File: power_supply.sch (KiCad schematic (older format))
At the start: 0 parts

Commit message: MSP73833 circuit stuff
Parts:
- added C? (x2): 4.7uF, symbol C
- added J?: USB, ~, symbol USB
- added LD? (x3): LED, ~, symbol LED
- added R? (x3): 1.5K, symbol R
- added R?: 1K, symbol R
- added RT?: 10K, symbol THERMISTOR
- added U?: MCP73833, ~, symbol MCP73833
- added U?: BATT, symbol BATT
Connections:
- net labels added: VBAT, VDD, VSS
- wire segments 0 -> 27
- no-connect marks 0 -> 3
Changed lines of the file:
@@
 LIBS:w_rtx
 LIBS:w_transistor
+LIBS:power_supply
 LIBS:power_supply-cache
 EELAYER 27 0
@@
 Comment4 ""
 $EndDescr
+$Comp
+L MCP73833 U?
+U 1 1 539B5EF0
+P 3500 2950
+F 0 "U?" H 3500 2650 60  0000 C CNN
+F 1 "MCP73833" H 3500 3250 60  0000 C CNN
+F 2 "~" H 3500 2800 60  0000 C CNN
+F 3 "~" H 3500 2800 60  0000 C CNN
+	1    3500 2950
+	1    0    0    -1
+$EndComp
+$Comp
+L USB J?
+U 1 1 539B5F0C
+P 1150 1250
+F 0 "J?" H 950 1250 60  0000 C CNN
+F 1 "USB" H 900 1600 60  0000 C CNN
+F 2 "~" H 1050 1350 60  0000 C CNN
+F 3 "~" H 1050 1350 60  0000 C CNN
+	1    1150 1250
+	1    0    0    -1
+$EndComp
+Text Label 1700 1450 0    60   ~ 0
+VSS
+Text Label 1700 1050 0    60   ~ 0
+VDD
+NoConn ~ 1600 1150
+NoConn ~ 1600 1250
+NoConn ~ 1600 1350
+Text Label 1900 2800 2    60   ~ 0
+VDD
+$Comp
+L C C?
+U 1 1 539B5F60
+P 2000 2900
+F 0 "C?" H 2050 2910 50  0000 L CNN
+F 1 "4.7uF" H 2050 2840 50  0000 L CNN
+F 2 "" H 2000 2900 60  0000 C CNN
+F 3 "" H 2000 2900 60  0000 C CNN
+	1    2000 2900
+	1    0    0    -1
+$EndComp
+Text Label 2000 3050 3    60   ~ 0
+VSS
+$Comp
+L C C?
+U 1 1 539B5FA3
+P 5100 2900
+F 0 "C?" H 5150 2910 50  0000 L CNN
+F 1 "4.7uF" H 5150 2840 50  0000 L CNN
+F 2 "" H 5100 2900 60  0000 C CNN
+F 3 "" H 5100 2900 60  0000 C CNN
+	1    5100 2900
+	1    0    0    -1
+$EndComp
+Text Label 5100 3050 3    60   ~ 0
+VSS
+$Comp
+L R R?
+U 1 1 539B5FBE
+P 2700 2950
+F 0 "R?" V 2750 2800 50  0000 C CNN
+F 1 "1.5K" V 2750 2950 50  0000 C CNN
+F 2 "" H 2700 2950 60  0000 C CNN
+F 3 "" H 2700 2950 60  0000 C CNN
+	1    2700 2950
+	0    -1   -1   0
+$EndComp
+$Comp
+L R R?
+U 1 1 539B5FCB
+P 2700 3050
+F 0 "R?" V 2750 2900 50  0000 C CNN
+F 1 "1.5K" V 2750 3050 50  0000 C CNN
+F 2 "" H 2700 3050 60  0000 C CNN
+F 3 "" H 2700 3050 60  0000 C CNN
+	1    2700 3050
+	0    -1   -1   0
+$EndComp
+$Comp
+L R R?
+U 1 1 539B5FD1
+P 4300 3050
+F 0 "R?" V 4350 2900 50  0000 C CNN
+F 1 "1.5K" V 4350 3050 50  0000 C CNN
+F 2 "" H 4300 3050 60  0000 C CNN
+F 3 "" H 4300 3050 60  0000 C CNN
+	1    4300 3050
+	0    1    1    0
+$EndComp
+$Comp
+L LED LD?
+U 1 1 539B6061
+P 2450 2950
+F 0 "LD?" H 2400 3000 40  0000 C CNN
+F 1 "LED" H 2550 3000 40  0000 C CNN
+F 2 "~" H 2450 2950 60  0000 C CNN
+F 3 "~" H 2450 2950 60  0000 C CNN
+	1    2450 2950
+	-1   0    0    1
+$EndComp
+$Comp
+L LED LD?
+U 1 1 539B6067
+P 2450 3050
+F 0 "LD?" H 2400 3100 40  0000 C CNN
+F 1 "LED" H 2550 3100 40  0000 C CNN
+F 2 "~" H 2450 3050 60  0000 C CNN
+F 3 "~" H 2450 3050 60  0000 C CNN
+	1    2450 3050
+	-1   0    0    1
+$EndComp
+$Comp
+L LED LD?
+U 1 1 539B606D
+P 4550 3050
+F 0 "LD?" H 4500 3100 40  0000 C CNN
+F 1 "LED" H 4650 3100 40  0000 C CNN
+F 2 "~" H 4550 3050 60  0000 C CNN
+F 3 "~" H 4550 3050 60  0000 C CNN
+	1    4550 3050
+	1    0    0    -1
+$EndComp
+$Comp
+L R R?
+U 1 1 539B617E
+P 4100 3350
+F 0 "R?" V 4150 3350 50  0000 C CNN
+F 1 "1K" V 4050 3350 50  0000 C CNN
+F 2 "" H 4100 3350 60  0000 C CNN
+F 3 "" H 4100 3350 60  0000 C CNN
+	1    4100 3350
+	1    0    0    -1
+$EndComp
+Text Label 4100 3550 3    60   ~ 0
+VSS
+Text Label 2800 3150 2    60   ~ 0
+VSS
+Text Label 4750 3050 0    60   ~ 0
+VDD
+Wire Wire Line
+	1600 1450 1700 1450
+Wire Wire Line
+	1600 1050 1700 1050
+Wire Wire Line
+	2900 2850 2900 2750
+Wire Wire Line
+	1900 2800 2900 2800
+Connection ~ 2900 2800
+Wire Wire Line
+	2000 2850 2000 2800
+Connection ~ 2000 2800
+Wire Wire Line
+	2000 3000 2000 3050
+Wire Wire Line
+	4100 2750 4100 2850
+Wire Wire Line
+	4100 2800 5650 2800
+Connection ~ 4100 2800
+Wire Wire Line
+	5100 2850 5100 2800
+Wire Wire Line
+	5100 3000 5100 3050
+Connection ~ 5100 2800
+Wire Wire Line
+	2900 2950 2800 2950
+Wire Wire Line
+	2800 3050 2900 3050
+Wire Wire Line
+	4100 3050 4200 3050
+Wire Wire Line
+	4400 3050 4450 3050
+Wire Wire Line
+	2550 3050 2600 3050
+Wire Wire Line
+	2600 2950 2550 2950
+Wire Wire Line
+	2350 2950 2350 2800
+Connection ~ 2350 2800
+Wire Wire Line
+	2300 2800 2300 3050
+Wire Wire Line
+	2300 3050 2350 3050
+Connection ~ 2300 2800
+Wire Wire Line
+	4650 3050 4750 3050
+Wire Wire Line
+	4100 3250 4100 3150
+Wire Wire Line
+	4100 3450 4100 3550
+Wire Wire Line
+	2900 3150 2800 3150
+Wire Wire Line
+	4100 2950 4200 2950
+$Comp
+L THERMISTOR RT?
+U 1 1 539B6353
+P 4400 2950
+F 0 "RT?" V 4450 2750 60  0000 C CNN
+F 1 "10K" V 4450 3050 60  0000 C CNN
+F 2 "" H 4400 2950 60  0000 C CNN
+F 3 "" H 4400 2950 60  0000 C CNN
+	1    4400 2950
+	0    -1   -1   0
+$EndComp
+Text Label 4750 2950 0    60   ~ 0
+VSS
+Wire Wire Line
+	4750 2950 4650 2950
+$Comp
+L BATT U?
+U 1 1 539B649A
+P 5600 2950
+F 0 "U?" V 5675 2925 60  0000 C CNN
+F 1 "BATT" V 5550 2925 60  0000 C CNN
+F 2 "" H 5600 2950 60  0000 C CNN
+F 3 "" H 5600 2950 60  0000 C CNN
+	1    5600 2950
+	1    0    0    -1
+$EndComp
+Wire Wire Line
+	5600 2800 5600 2850
+Text Label 5650 2800 0    60   ~ 0
+VBAT
+Connection ~ 5600 2800
+Text Label 5600 3150 3    60   ~ 0
+VSS
+Wire Wire Line
+	5600 3100 5600 3150
 $EndSCHEMATC

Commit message: Updated library. Began adding components.
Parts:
- added R?: 100k, symbol R
- added U?: FDC6392S, symbol FDC6392S
- added U?: MIC2185, symbol MIC2185
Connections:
- net labels added: VSYS
- wire segments 27 -> 35
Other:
- moved on the sheet: C?, J?, LD?, R?, RT?, U?

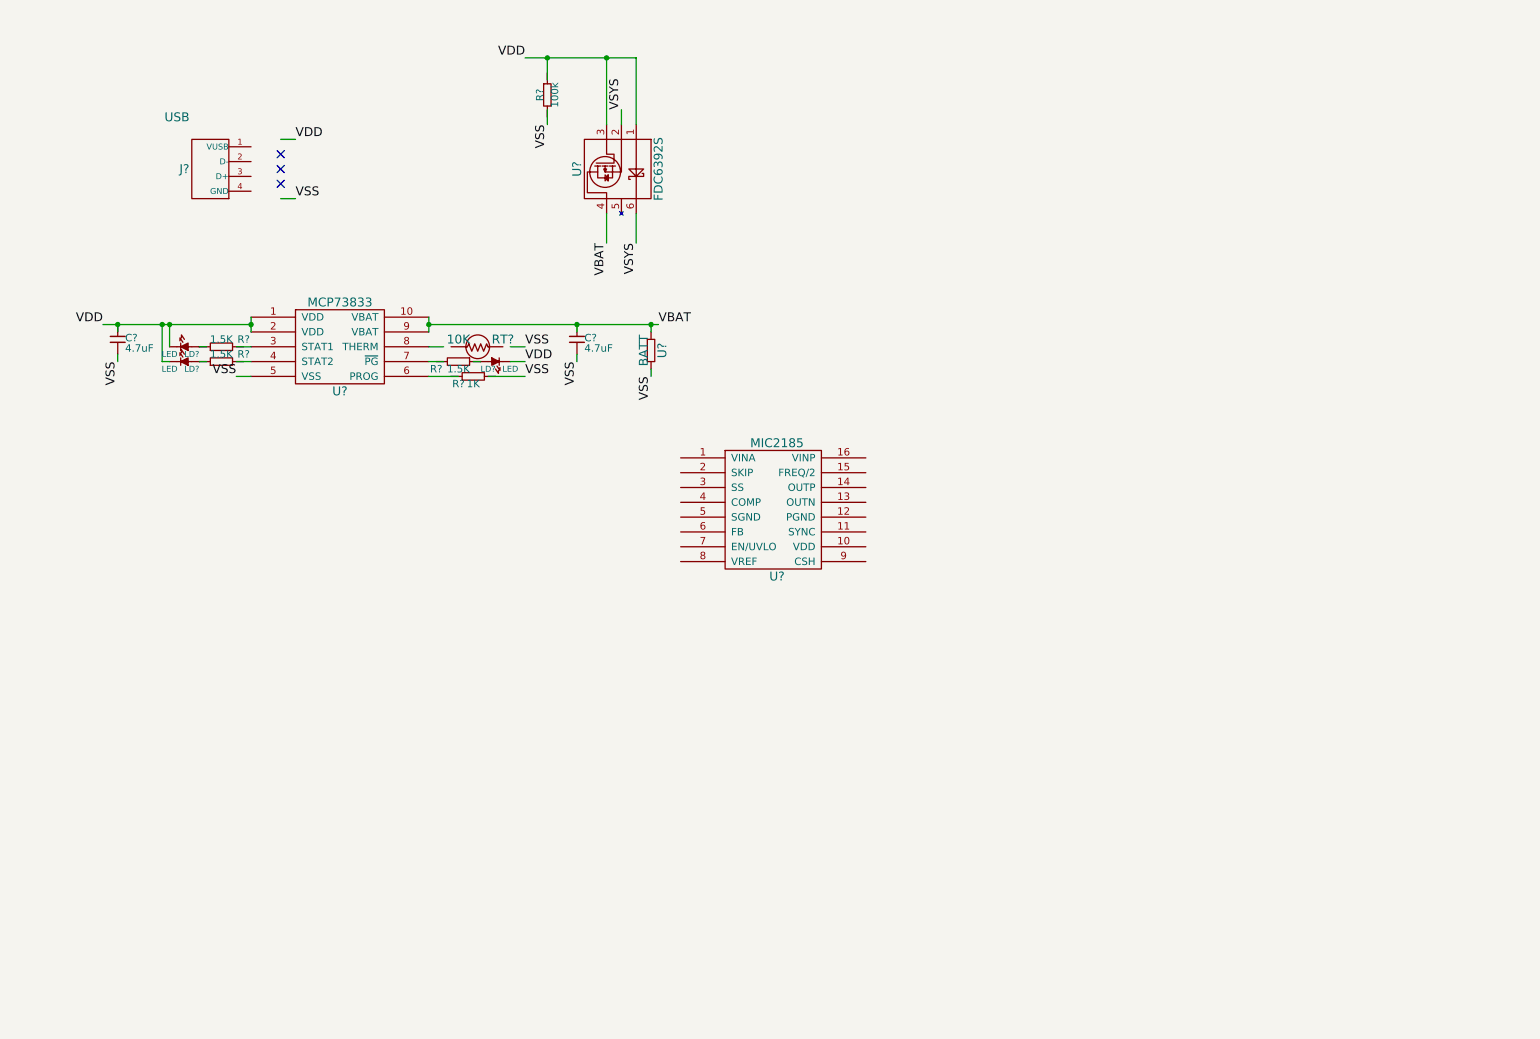
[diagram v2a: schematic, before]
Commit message: Power Supply Schematic
Completed schematic up through the MIC2185

Regulated output voltage named VpREG

Custom components listed in power_supply-cache.lib
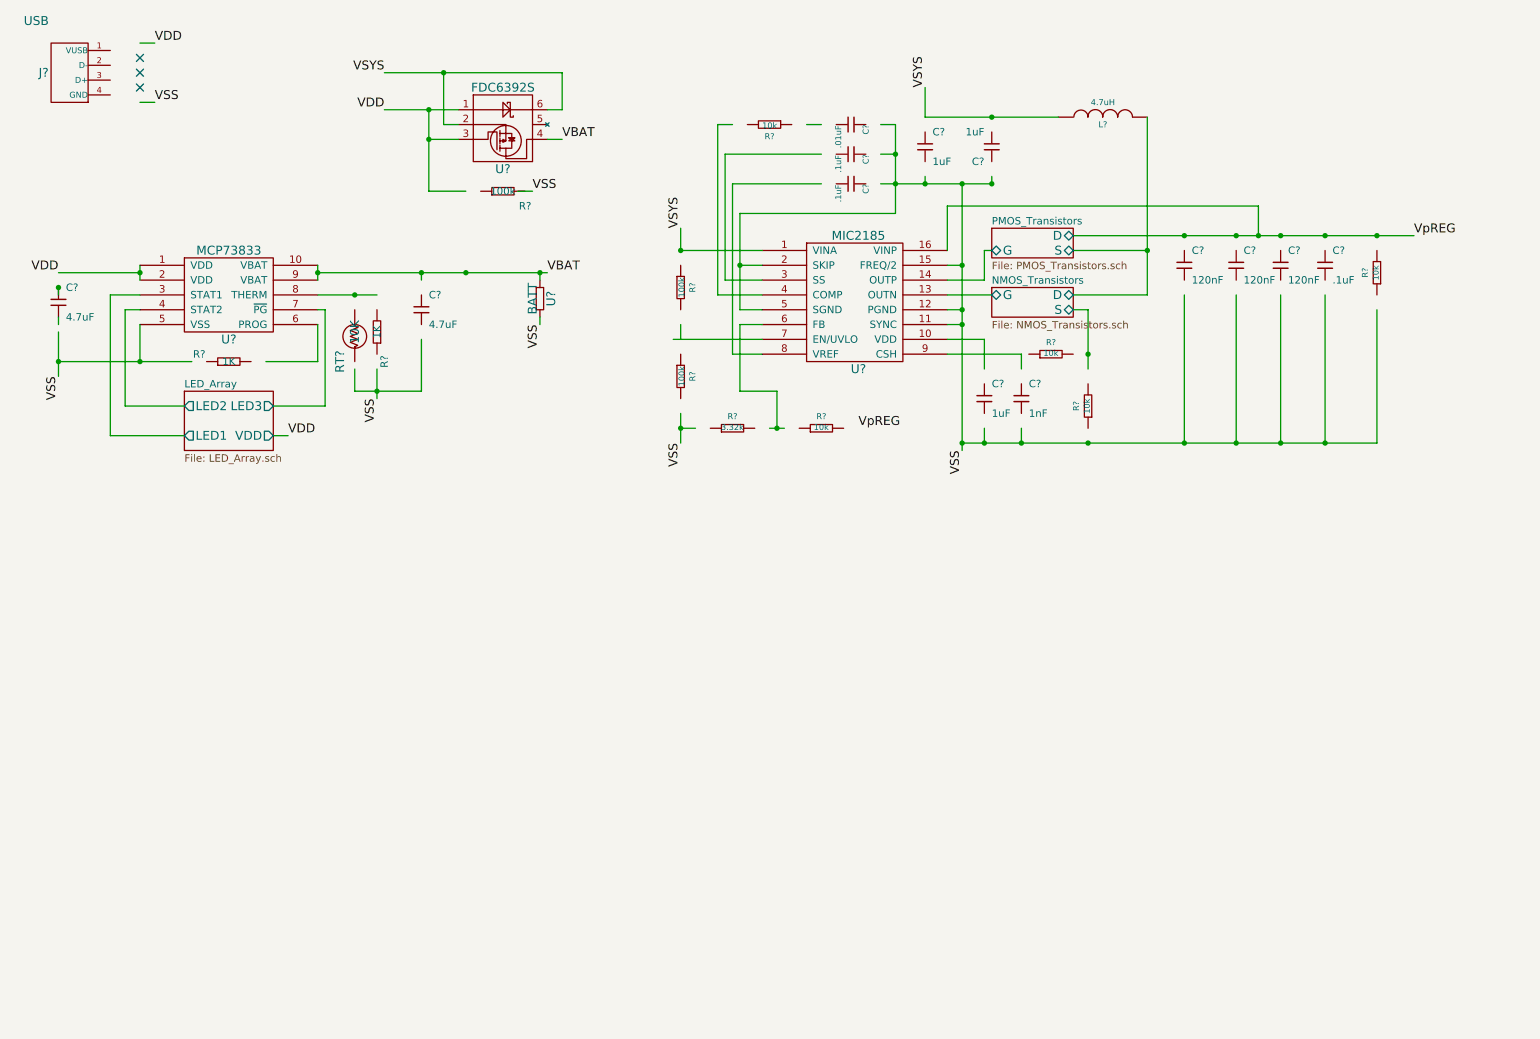
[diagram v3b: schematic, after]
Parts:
- removed LD? (x3): LED, ~, symbol LED
- removed R? (x3): 1.5K, symbol R
- added C? (x2): .1uF, ~, symbol C
- added C?: .01uF, ~, symbol C
- added C? (x3): 1uF, symbol C
- added C?: 1nF, symbol C
- added C? (x3): 120nF, symbol C
- added C?: .1uF, symbol C
- added L?: 4.7uH, ~, symbol INDUCTOR
- added R?: 1K, symbol R
- added R? (x2): 100k, ~, symbol R
- added R? (x5): 10k, ~, symbol R
- added R?: 3.32k, ~, symbol R
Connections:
- net labels added: VpREG
- wire segments 35 -> 104
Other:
- moved on the sheet: C?, J?, R?, RT?, U?

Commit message: Updated component library
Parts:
- removed J?: USB, ~, symbol USB
- added U?: USB-MICRO, symbol USB-MICRO
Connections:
- wire segments 104 -> 114
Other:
- moved on the sheet: C?, R?

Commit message: Finished schematic
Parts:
- removed C? (x2): 4.7uF, symbol C
- removed C? (x2): .1uF, ~, symbol C
- removed C?: .01uF, ~, symbol C
- removed C? (x3): 1uF, symbol C
- removed C?: 1nF, symbol C
- removed C? (x3): 120nF, symbol C
- removed C?: .1uF, symbol C
- removed L?: 4.7uH, ~, symbol INDUCTOR
- removed R? (x2): 1K, symbol R
- removed R?: 100k, symbol R
- removed R? (x2): 100k, ~, symbol R
- removed R? (x5): 10k, ~, symbol R
- removed R?: 3.32k, ~, symbol R
- removed RT?: 10K, symbol THERMISTOR
- removed U?: MCP73833, ~, symbol MCP73833
- removed U?: BATT, symbol BATT
- removed U?: FDC6392S, symbol FDC6392S
- removed U?: MIC2185, symbol MIC2185
- added C? (x4): .1uF, symbol C
- added C?: .01uF, symbol C
- added C?: 1nF, symbol C
- added C?: 1uF, symbol C
- added C?: 47uF, symbol C
- added C? (x3): 120uF, symbol C
- added C? (x2): 4.7uF, symbol C
- added D?: B130, symbol SCHOTTKY
- added D? (x13): LED, ~, symbol LED
- added D?: SCHOTTKY, symbol SCHOTTKY
- added F?: PTC, symbol PTC
- added J?: USB, ~, symbol USB
- added L?: 4.7uH, ~, symbol INDUCTOR
- added Q? (x2): SI4174DY, ~, symbol SI4174DY
- added Q? (x2): SI4463CDY, ~, symbol SI4463CDY
- added R? (x6): 100k, ~, symbol R
- added R?: 10k, ~, symbol R
- added R?: .010, ~, symbol R
- added R?: 3.32k, ~, symbol R
- added R?: .025, ~, symbol R
- added R? (x2): 26.1, ~, symbol R
- added R? (x2): 100k, symbol POT
- added R?: 130k, ~, symbol R
- added R?: 4.8k, ~, symbol R
- added R?: 1K, symbol R
- added R?: 100k, symbol R
- added R? (x3): 1.5k, ~, symbol R
- added RT?: 10K, symbol THERMISTOR
- added U?: MIC2185, symbol MIC2185
- added U?: LM3914, symbol LM3914
- added U?: MAX9938, symbol MAX9938
- added U?: MCP73833, ~, symbol MCP73833
- added U?: BATT, symbol BATT
- added U?: FDC6392S, symbol FDC6392S
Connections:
- net VBAT: now also C?.1, U?.10 (VBAT), U?.4, U?.9 (VBAT), U?.~
- net VDD: now also C?.1, R?.1, R?.1, R?.2, R?.2, U?.1, U?.1 (VDD), U?.2 (VDD), U?.3
- net VSS: now also C?.2, C?.2, C?.2, C?.2, C?.2, C?.2, C?.2, C?.2, C?.2, C?.2, C?.2, C?.2, C?.2, J?.4 (GND), R?.1, R?.1, R?.1, R?.1, R?.1, R?.2, R?.2, R?.2, R?.2, R?.3, RT?.2, U?.1 (GND), U?.11 (SYNC), U?.12 (PGND), U?.2 (GND), U?.2 (SKIP), U?.2 (V-), U?.4 (RLO), U?.5 (SGND), U?.5 (VSS), U?.9 (MODE), U?.~
- net VSYS: now also C?.1, C?.1, L?.1, R?.1, U?.1 (VINA), U?.2, U?.6
- new net: C?.1, U?.10 (VDD), U?.15 (FREQ/2)
- new net: Q?.G, Q?.G, U?.13 (OUTN)
- new net: Q?.G, Q?.G, U?.14 (OUTP)
- new net: C?.1, U?.3 (SS)
- new net: R?.1, U?.4 (COMP)
- new net: R?.1, R?.2, U?.6 (FB)
- new net: R?.1, R?.2, U?.7 (EN/UVLO)
- new net: C?.1, U?.8 (VREF)
- new net: C?.1, R?.1, U?.9 (CSH)
- new net: C?.1, R?.2
- new net: D?.1, L?.2, Q?.D, Q?.D, Q?.D, Q?.D
- new net: Q?.S, Q?.S, R?.1, R?.2
- new net: D?.2 (K), U?.1 (LED1)
- new net: D?.2 (K), U?.10 (LED10)
- new net: D?.2 (K), U?.11 (LED9)
- new net: D?.2 (K), U?.12 (LED8)
- new net: D?.2 (K), U?.13 (LED7)
- new net: D?.2 (K), U?.14 (LED6)
- new net: D?.2 (K), U?.15 (LED5)
- new net: D?.2 (K), U?.16 (LED4)
- new net: D?.2 (K), U?.17 (LED3)
- new net: D?.2 (K), U?.18 (LED2)
- new net: R?.2, U?.6 (RHI), U?.7 (REFOUT)
- new net: R?.1, R?.2, U?.8 (REFADJ)
- new net: D?.1, R?.2, U?.4 (RS-)
- new net: D?.2, F?.1
- new net: D?.1 (A), U?.3 (STAT1)
- new net: D?.1 (A), U?.4 (STAT2)
- new net: R?.2, U?.6 (PROG)
- new net: D?.1 (A), U?.7 (~PG)
- new net: RT?.1, U?.8 (THERM)
- new net: D?.2 (K), R?.2 (x2)
- new net: D?.2 (K), R?.1
- new net D+: J?.3 (D+), R?.1, R?.1, R?.2, R?.2
- new net D-: J?.2 (D-), R?.1, R?.2, R?.2, R?.3
- new net I_SENSE: U?.3 (OUT), U?.5 (SIG)
- new net VOUT: F?.2, J?.1 (VUSB), R?.1, R?.2
- new net VREG: C?.1, C?.1, C?.1, C?.1, D?.1 (A), D?.1 (A), D?.1 (A), D?.1 (A), D?.1 (A), D?.1 (A), D?.1 (A), D?.1 (A), D?.1 (A), D?.1 (A), D?.2, Q?.S, Q?.S, R?.1, R?.1, U?.16 (VINP), U?.3 (V+), U?.5 (RS+)
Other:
- note added: "187.5 mV per step dot display driver \n2mA output per LED\n"
- note added: "Full Scale Voltage: 1.875V"
- note added: "Non Inductive Resistor"
- moved on the sheet: U?

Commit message: Added ESD protection to input and output.
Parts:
- removed D?: SCHOTTKY, symbol SCHOTTKY
- added U? (x2): TPD2E001DRL, symbol TPD2E001DRL
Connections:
- net D+: now also U?.5 (IO2)
- net D-: now also U?.3 (IO1)
- net VDD: now also U?.1 (VCC)
- net VOUT: now also U?.1 (VCC)
- net VSS: now also U?.4 (GND), U?.4 (GND)
- net at U?.2 (D-): now also U?.3 (IO1)
- net at U?.3 (D+): now also U?.5 (IO2)
- net at R?.2, U?.4 (RS-): now also F?.1
- no-connect marks 3 -> 1
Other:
- moved on the sheet: F?, J?
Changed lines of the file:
@@
 Sheet 1 1
 Title "5V Battery Power Supply"
-Date "16 jun 2014"
+Date "17 jun 2014"
 Rev "2"
 Comp "AMP Lab"
@@
 Text Label 1775 1625 0    60   ~ 0
 VDD
-NoConn ~ 1675 1725
-NoConn ~ 1675 1825
 NoConn ~ 1675 1925
 $Comp
@@
 L USB J?
 U 1 1 53A02AE3
-P 9425 6225
-F 0 "J?" V 9375 6225 60  0000 C CNN
-F 1 "USB" H 9425 6475 60  0000 C CNN
-F 2 "~" H 9425 6075 60  0000 C CNN
-F 3 "~" H 9425 6075 60  0000 C CNN
-	1    9425 6225
-	1    0    0    -1
-$EndComp
-Text Label 9825 6075 0    60   ~ 0
+P 9875 5975
+F 0 "J?" V 9825 5975 60  0000 C CNN
+F 1 "USB" H 9875 6225 60  0000 C CNN
+F 2 "~" H 9875 5825 60  0000 C CNN
+F 3 "~" H 9875 5825 60  0000 C CNN
+	1    9875 5975
+	1    0    0    -1
+$EndComp
+Text Label 10275 5825 0    60   ~ 0
 VOUT
-Text Label 9825 6375 0    60   ~ 0
+Text Label 10275 6125 0    60   ~ 0
 VSS
-Text Label 9825 6175 0    60   ~ 0
+Text Label 10275 5925 0    60   ~ 0
 D-
-Text Label 9825 6275 0    60   ~ 0
+Text Label 10275 6025 0    60   ~ 0
 D+
 $Comp
@@
 $EndComp
 $Comp
-L SCHOTTKY D?
-U 1 1 53A07598
-P 9850 4350
-F 0 "D?" H 9950 4300 40  0000 C CNN
-F 1 "SCHOTTKY" H 9850 4400 40  0000 C CNN
-F 2 "" H 9850 4350 60  0000 C CNN
-F 3 "" H 9850 4350 60  0000 C CNN
-	1    9850 4350
-	1    0    0    -1
-$EndComp
-$Comp
 L MCP73833 U?
 U 1 1 53A080EC
@@
 	2050 7225 1900 7225
 Wire Wire Line
-	9675 6075 9825 6075
-Wire Wire Line
-	9675 6375 9825 6375
-Wire Wire Line
-	9675 6175 9825 6175
-Wire Wire Line
-	9675 6275 9825 6275
+	10125 5825 10275 5825
+Wire Wire Line
+	10125 6125 10275 6125
+Wire Wire Line
+	10125 5925 10275 5925
+Wire Wire Line
+	10125 6025 10275 6025
 Wire Wire Line
 	6050 6225 6050 6125
@@
 L PTC F?
 U 1 1 53A0B4AA
-P 10250 4350
-F 0 "F?" H 10300 4300 40  0000 C CNN
-F 1 "PTC" H 10150 4375 40  0000 C CNN
-F 2 "" H 10250 4350 60  0000 C CNN
-F 3 "" H 10250 4350 60  0000 C CNN
-	1    10250 4350
+P 9900 4350
+F 0 "F?" H 9950 4300 40  0000 C CNN
+F 1 "PTC" H 9800 4375 40  0000 C CNN
+F 2 "" H 9900 4350 60  0000 C CNN
+F 3 "" H 9900 4350 60  0000 C CNN
+	1    9900 4350
 	1    0    0    -1
 $EndComp
@@
 Connection ~ 9550 4350
 Wire Wire Line
-	10100 4350 9950 4350
-Wire Wire Line
-	10400 4350 10525 4350
-Text Label 10525 4350 0    60   ~ 0
+	10050 4350 10175 4350
+Text Label 10175 4350 0    60   ~ 0
 VOUT
+$Comp
+L TPD2E001DRL U?
+U 1 1 539F96A5
+P 2650 1825
+F 0 "U?" H 2750 1825 40  0000 C CNN
+F 1 "TPD2E001DRL" H 2650 2025 40  0000 C CNN
+F 2 "" H 2650 1825 60  0000 C CNN
+F 3 "" H 2650 1825 60  0000 C CNN
+	1    2650 1825
+	0    1    1    0
+$EndComp
+$Comp
+L TPD2E001DRL U?
+U 1 1 539F96B2
+P 8475 5975
+F 0 "U?" H 8575 5975 40  0000 C CNN
+F 1 "TPD2E001DRL" H 8475 6175 40  0000 C CNN
+F 2 "" H 8475 5975 60  0000 C CNN
+F 3 "" H 8475 5975 60  0000 C CNN
+	1    8475 5975
+	1    0    0    -1
+$EndComp
+Wire Wire Line
+	2550 2125 2550 2200
+Wire Wire Line
+	2550 2200 2100 2200
+Wire Wire Line
+	2100 2200 2100 1825
+Wire Wire Line
+	2100 1825 1675 1825
+Wire Wire Line
+	1675 1725 2100 1725
+Wire Wire Line
+	2100 1725 2100 1425
+Wire Wire Line
+	2100 1425 2550 1425
+Wire Wire Line
+	2550 1425 2550 1525
+Wire Wire Line
+	2750 1525 2750 1425
+Text Label 2750 1425 1    60   ~ 0
+VDD
+Text Label 2750 2225 3    60   ~ 0
+VSS
+Wire Wire Line
+	2750 2125 2750 2225
+Text Label 8925 5875 0    60   ~ 0
+VSS
+Wire Wire Line
+	8775 5875 8925 5875
+Text Label 8025 5875 2    60   ~ 0
+VOUT
+Wire Wire Line
+	8025 5875 8175 5875
+Text Label 8925 6075 0    60   ~ 0
+D+
+Text Label 8025 6075 2    60   ~ 0
+D-
+Wire Wire Line
+	8025 6075 8175 6075
+Wire Wire Line
+	8925 6075 8775 6075
 $EndSCHEMATC
